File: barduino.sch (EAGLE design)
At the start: 17 parts, among them Q2 16MHz, X1 MINI-USB-UX60A-MB-5ST

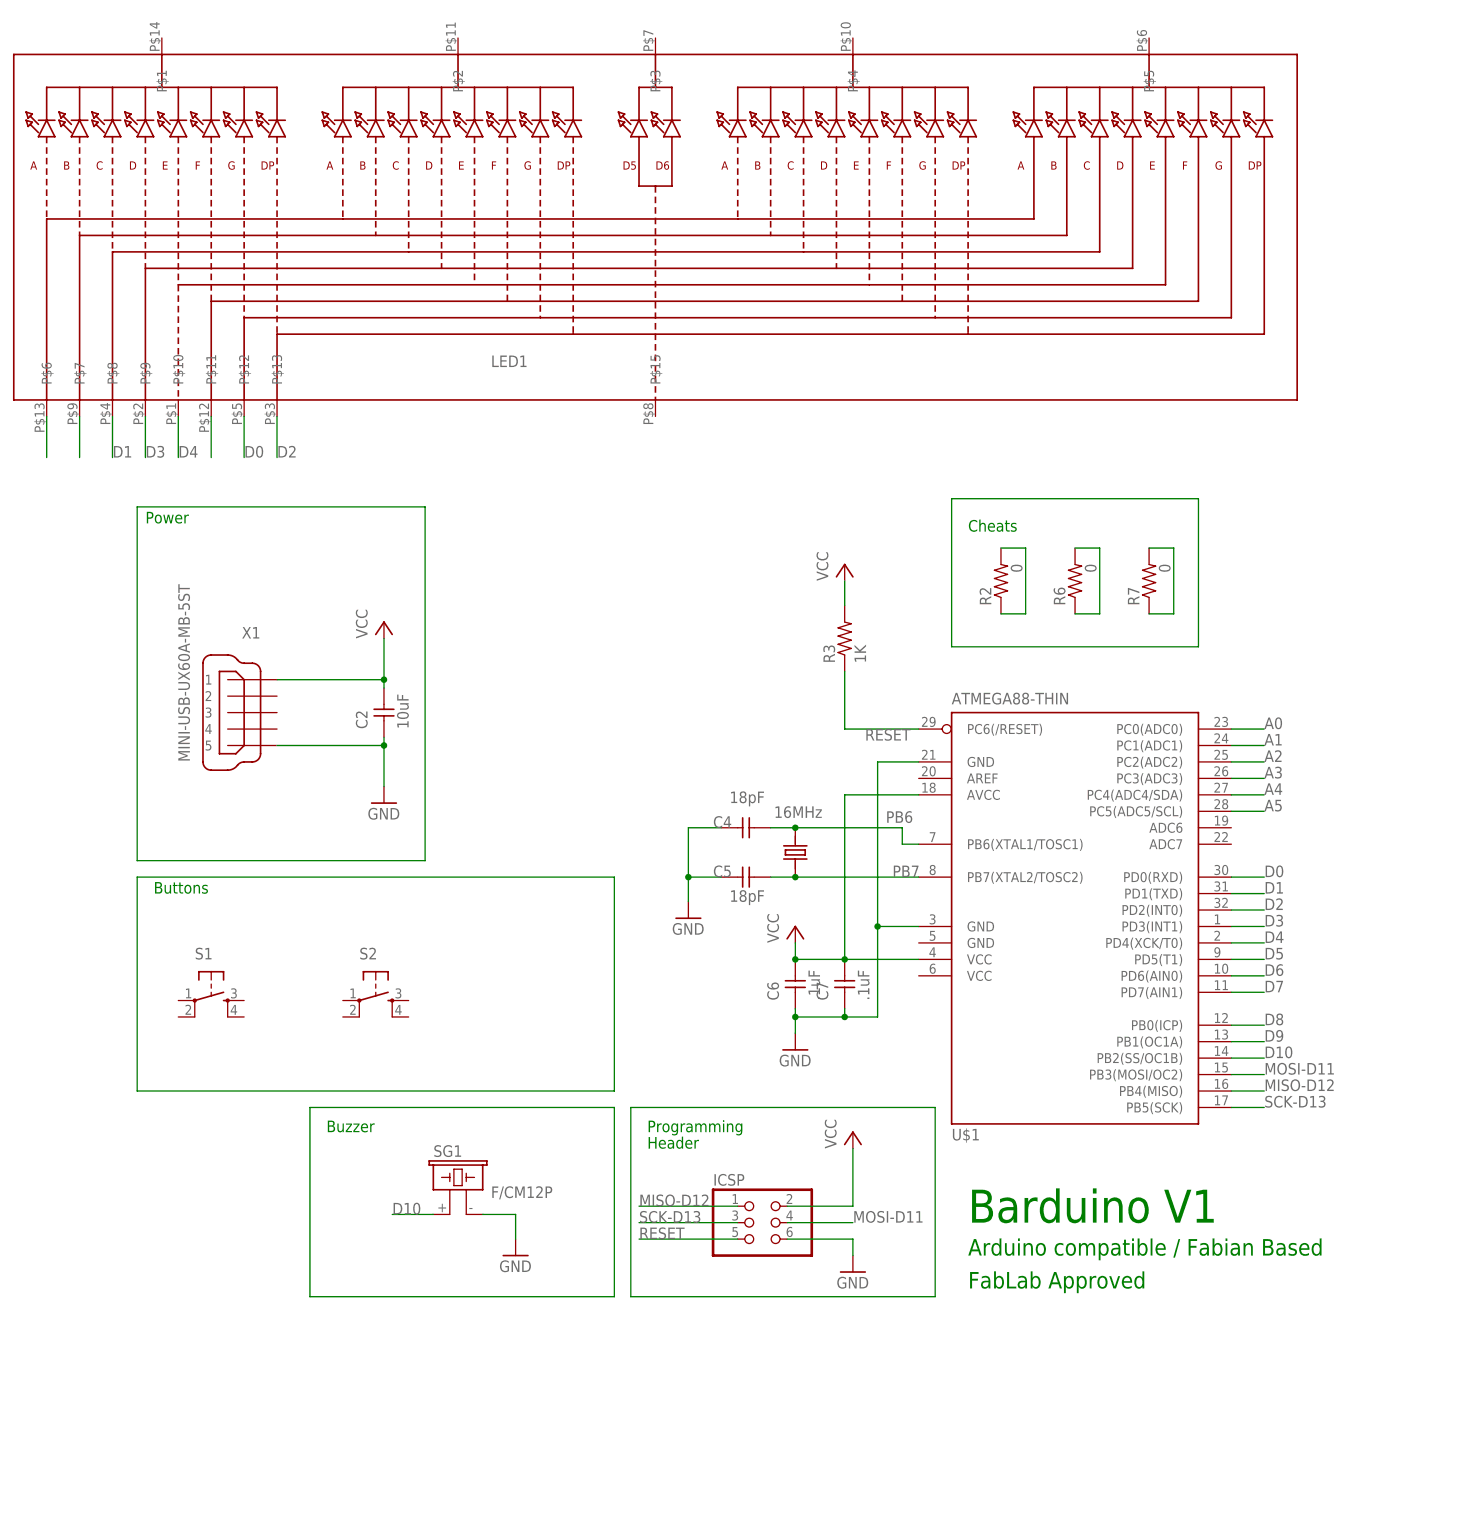
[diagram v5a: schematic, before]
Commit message: replace clock part with 2 custom headers
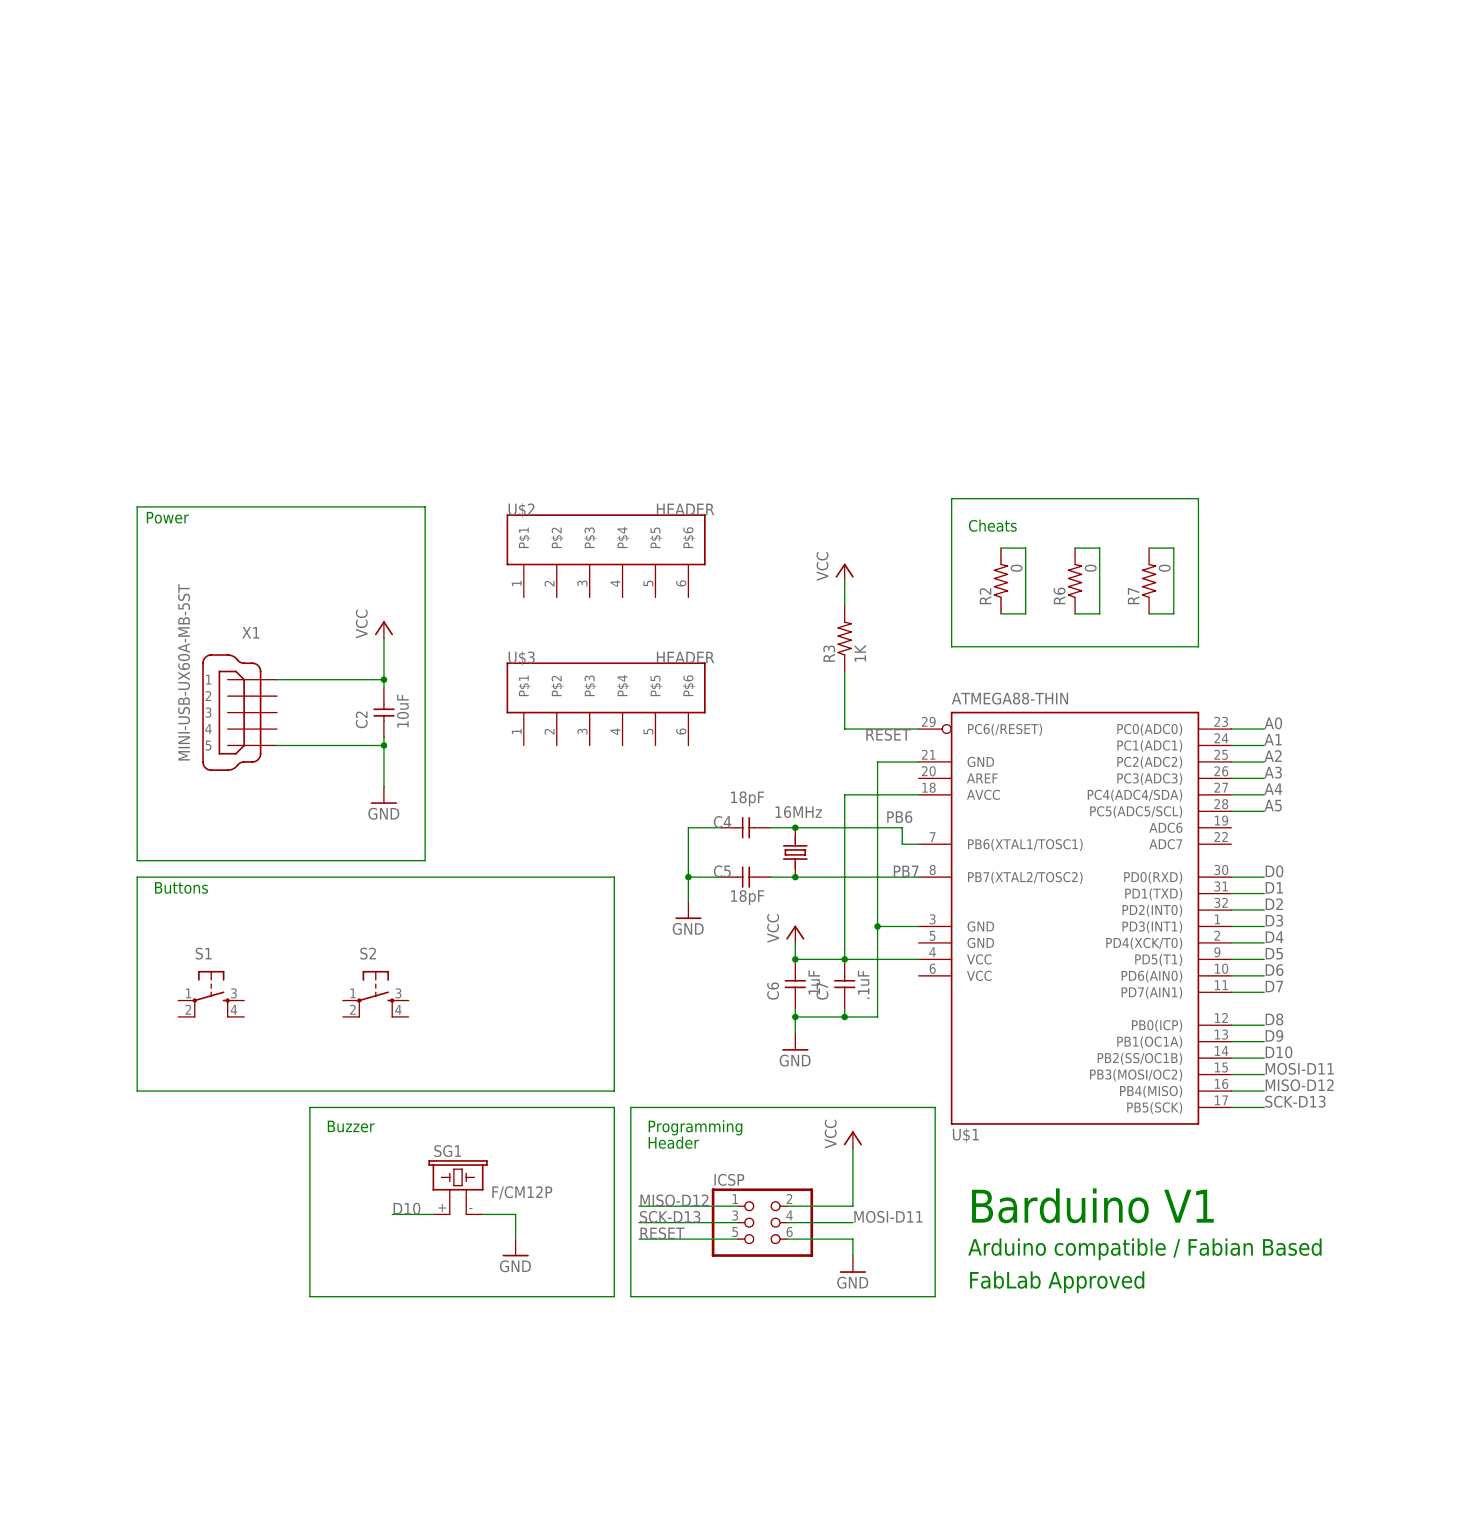
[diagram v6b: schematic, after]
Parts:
- removed LED1: (no value), microbuilder:DISP_SEGMENT_4DIGIT_BL-Q56C43
- added U$2, U$3: HEADER, 4-Digit-Clock:HEADER
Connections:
- removed net N$22: LED1.P$6
- removed net N$23: LED1.P$7
- removed net N$27: LED1.P$11
- net D0: no longer LED1.P$12
- net D1: no longer LED1.P$8
- net D2: no longer LED1.P$13
- net D3: no longer LED1.P$9
- net D4: no longer LED1.P$10
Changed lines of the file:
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@@
 <setting verticaltext="up"/>
 </settings>
-<grid distance="0.05" unitdist="inch" unit="inch" style="lines" multiple="1" display="no" altdistance="0.01" altunitdist="inch" altunit="inch"/>
+<grid distance="0.1" unitdist="inch" unit="inch" style="lines" multiple="1" display="no" altdistance="0.01" altunitdist="inch" altunit="inch"/>
 <layers>
 <layer number="1" name="Top" color="4" fill="1" visible="no" active="no"/>
@@
 <part name="R7" library="ng" deviceset="RESISTOR" device="1206" value="0"/>
 <part name="R2" library="ng" deviceset="RESISTOR" device="1206" value="0"/>
-<part name="LED1" library="microbuilder" deviceset="DISP_SEGMENT_4DIGIT_BL-Q56C43" device=""/>
 <part name="GND2" library="supply1" library_urn="urn:adsk.eagle:library:371" deviceset="GND" device=""/>
 <part name="SG1" library="buzzer" library_urn="urn:adsk.eagle:library:113" deviceset="F/CM12P" device=""/>
@@
 <part name="P+4" library="supply1" library_urn="urn:adsk.eagle:library:371" deviceset="VCC" device=""/>
 <part name="GND5" library="supply1" library_urn="urn:adsk.eagle:library:371" deviceset="GND" device=""/>
+<part name="U$2" library="4-Digit-Clock" deviceset="HEADER" device=""/>
+<part name="U$3" library="4-Digit-Clock" deviceset="HEADER" device=""/>
 </parts>
 <sheets>
@@
 <attribute name="VALUE" x="84.582" y="120.65" size="1.778" layer="96" rot="R90"/>
 </instance>
-<instance part="LED1" gate="G$1" x="27.94" y="170.18"/>
 <instance part="GND2" gate="1" x="6.35" y="15.24"/>
 <instance part="SG1" gate="G$1" x="-3.81" y="24.13"/>
@@
 <instance part="P+4" gate="VCC" x="58.42" y="34.29"/>
 <instance part="GND5" gate="1" x="58.42" y="12.7"/>
+<instance part="U$2" gate="G$1" x="20.32" y="127"/>
+<instance part="U$3" gate="G$1" x="20.32" y="104.14"/>
 </instances>
 <busses>
@@
 <pinref part="U$1" gate="G$1" pin="PD0(RXD)"/>
 </segment>
-<segment>
-<pinref part="LED1" gate="G$1" pin="P$12"/>
-<wire x1="-35.56" y1="144.78" x2="-35.56" y2="138.43" width="0.1524" layer="91"/>
-<label x="-35.56" y="138.43" size="1.778" layer="95"/>
-</segment>
 </net>
 <net name="D1" class="0">
@@
 <pinref part="U$1" gate="G$1" pin="PD1(TXD)"/>
 </segment>
-<segment>
-<pinref part="LED1" gate="G$1" pin="P$8"/>
-<wire x1="-55.88" y1="144.78" x2="-55.88" y2="138.43" width="0.1524" layer="91"/>
-<label x="-55.88" y="138.43" size="1.778" layer="95"/>
-</segment>
 </net>
 <net name="D2" class="0">
@@
 <pinref part="U$1" gate="G$1" pin="PD2(INT0)"/>
 </segment>
-<segment>
-<pinref part="LED1" gate="G$1" pin="P$13"/>
-<wire x1="-30.48" y1="144.78" x2="-30.48" y2="138.43" width="0.1524" layer="91"/>
-<label x="-30.48" y="138.43" size="1.778" layer="95"/>
-</segment>
 </net>
 <net name="D3" class="0">
@@
 <pinref part="U$1" gate="G$1" pin="PD3(INT1)"/>
 </segment>
-<segment>
-<pinref part="LED1" gate="G$1" pin="P$9"/>
-<wire x1="-50.8" y1="144.78" x2="-50.8" y2="138.43" width="0.1524" layer="91"/>
-<label x="-50.8" y="138.43" size="1.778" layer="95"/>
-</segment>
 </net>
 <net name="D4" class="0">
@@
 <label x="121.92" y="63.5" size="1.778" layer="95"/>
 <pinref part="U$1" gate="G$1" pin="PD4(XCK/T0)"/>
-</segment>
-<segment>
-<pinref part="LED1" gate="G$1" pin="P$10"/>
-<wire x1="-45.72" y1="144.78" x2="-45.72" y2="138.43" width="0.1524" layer="91"/>
-<label x="-45.72" y="138.43" size="1.778" layer="95"/>
 </segment>
 </net>
@@
 </segment>
 </net>
-<net name="N$22" class="0">
-<segment>
-<pinref part="LED1" gate="G$1" pin="P$6"/>
-<wire x1="-66.04" y1="144.78" x2="-66.04" y2="138.43" width="0.1524" layer="91"/>
-</segment>
-</net>
-<net name="N$23" class="0">
-<segment>
-<pinref part="LED1" gate="G$1" pin="P$7"/>
-<wire x1="-60.96" y1="144.78" x2="-60.96" y2="138.43" width="0.1524" layer="91"/>
-</segment>
-</net>
-<net name="N$27" class="0">
-<segment>
-<pinref part="LED1" gate="G$1" pin="P$11"/>
-<wire x1="-40.64" y1="144.78" x2="-40.64" y2="138.43" width="0.1524" layer="91"/>
-</segment>
-</net>

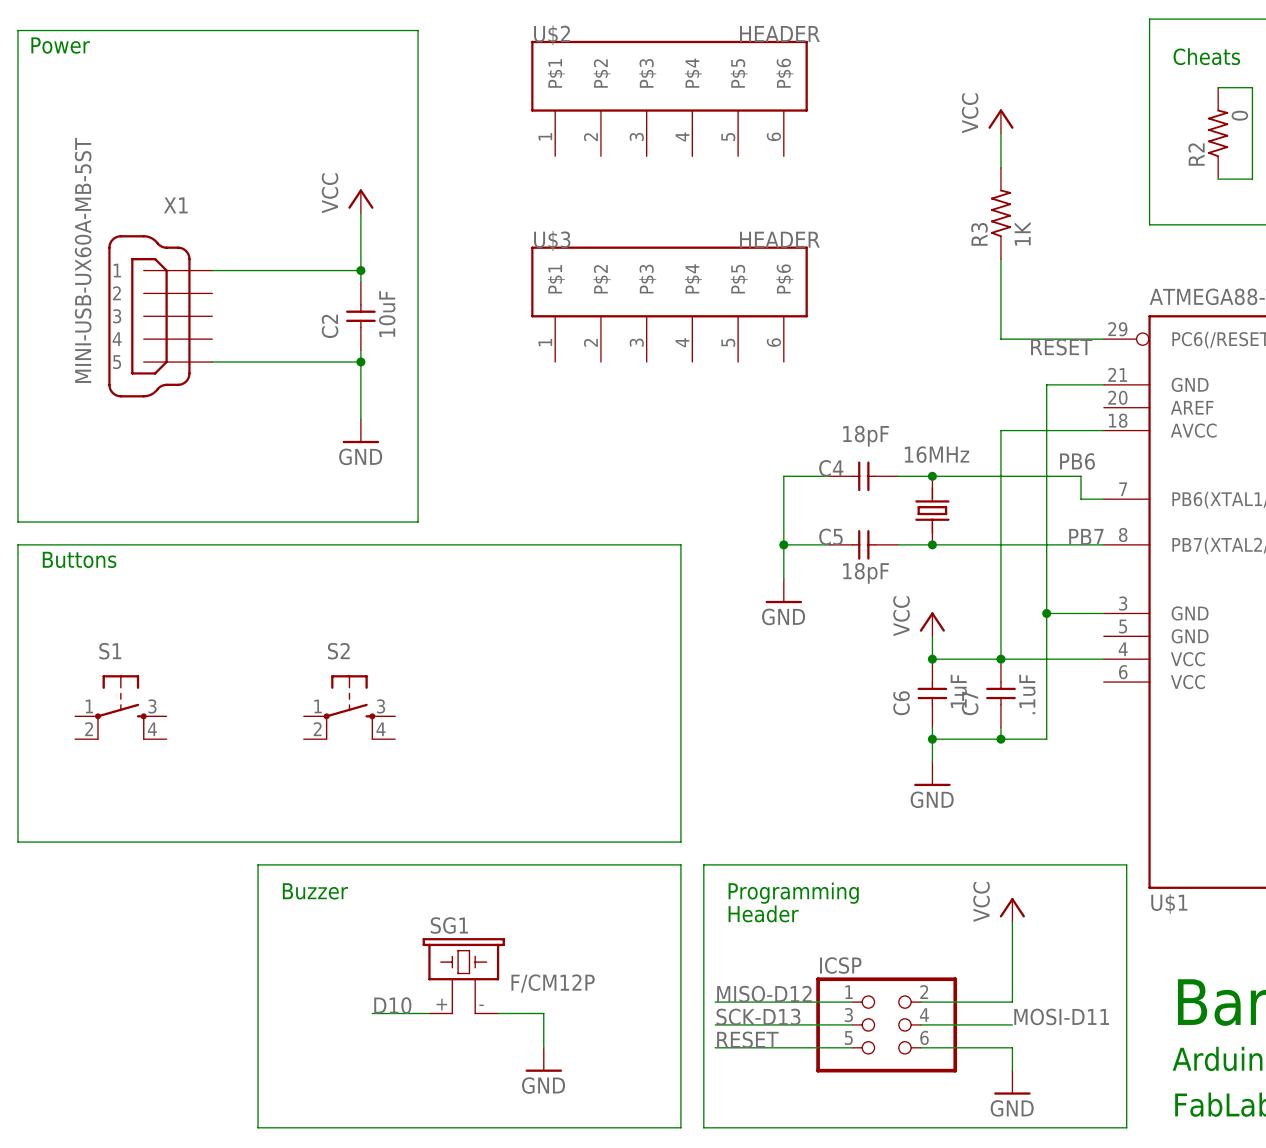
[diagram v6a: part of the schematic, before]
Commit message: display and buttons connected
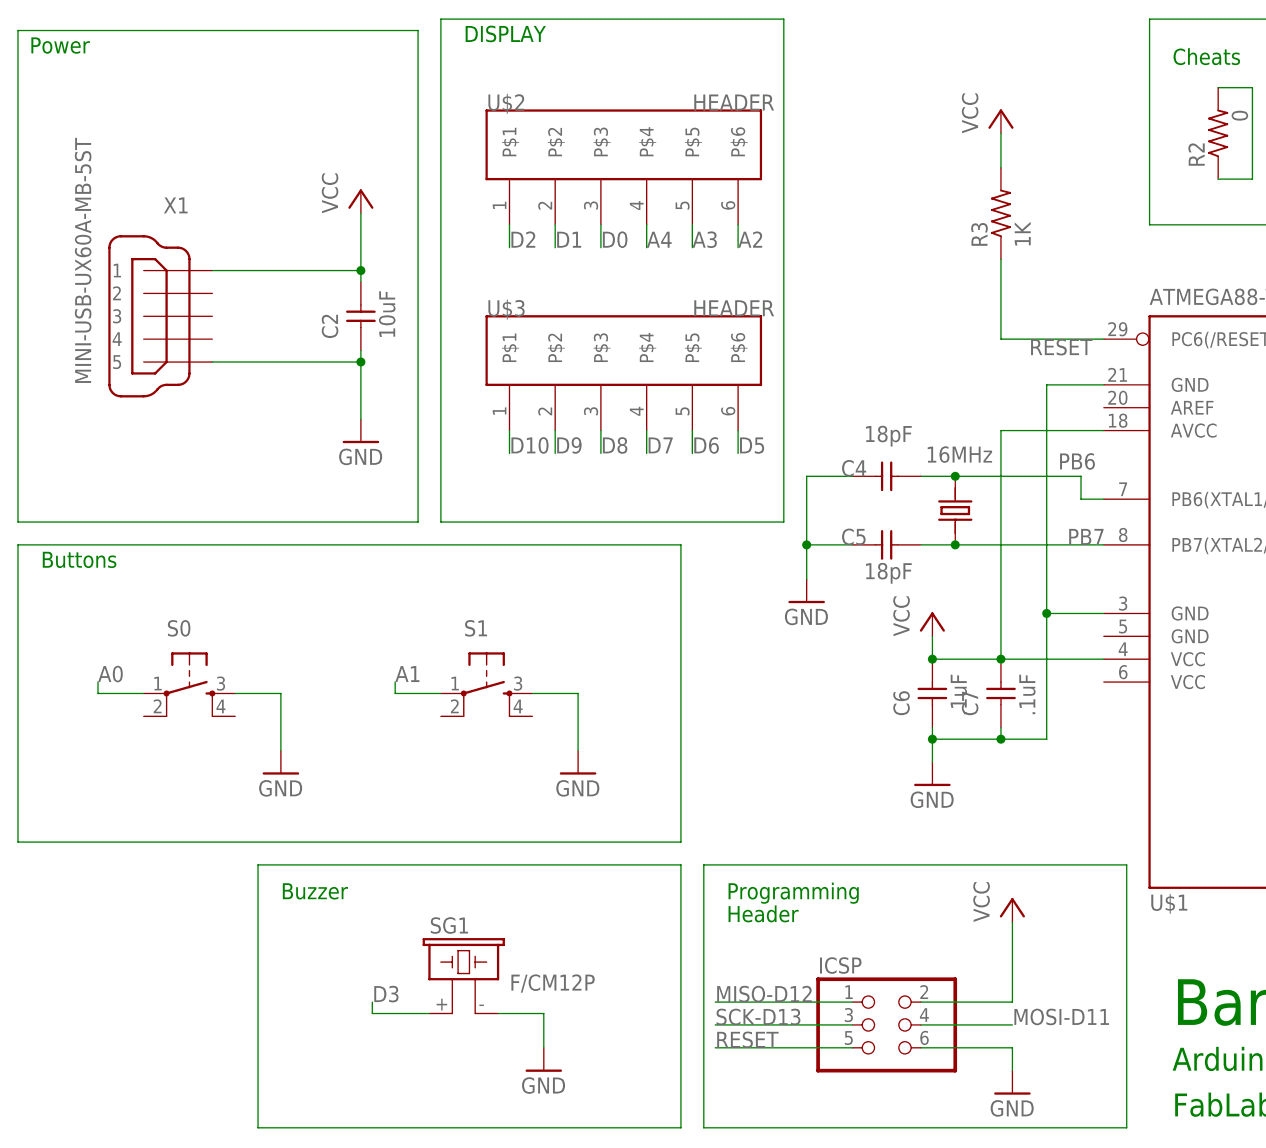
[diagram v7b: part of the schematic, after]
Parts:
- removed S2: (no value), ng:6MM_SWITCH6MM_SWITCH
- added S0: (no value), ng:6MM_SWITCH6MM_SWITCH
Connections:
- net A0: now also S0.P
- net A1: now also S1.P
- net A2: now also U$2.P$6
- net A3: now also U$2.P$5
- net A4: now also U$2.P$4
- net D0: now also U$2.P$3
- net D1: now also U$2.P$2
- net D10: now also U$3.P$1; no longer SG1.1
- net D2: now also U$2.P$1
- net D3: now also SG1.1
- net D5: now also U$3.P$6
- net D6: now also U$3.P$5
- net D7: now also U$3.P$4
- net D8: now also U$3.P$3
- net D9: now also U$3.P$2
- net GND: now also S0.S, S1.S
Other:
- note added: "DISPLAY"
- moved on the sheet: C4, C5, S1, U$2, U$3

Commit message: lots of routing
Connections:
- removed net N$3: R6.1, R6.2
- net SCK-D13: no longer R2.1, R2.2
- net VCC: no longer R7.1, R7.2
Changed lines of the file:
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@@
-</segment>
-<segment>
-<pinref part="R7" gate="G$1" pin="1"/>
-<wire x1="104.14" y1="114.3" x2="107.95" y2="114.3" width="0.1524" layer="91"/>
-<wire x1="107.95" y1="114.3" x2="107.95" y2="124.46" width="0.1524" layer="91"/>
-<pinref part="R7" gate="G$1" pin="2"/>
-<wire x1="107.95" y1="124.46" x2="104.14" y2="124.46" width="0.1524" layer="91"/>
 </segment>
 <segment>
@@
 <pinref part="ICSP" gate="A" pin="3"/>
 </segment>
-<segment>
-<pinref part="R2" gate="G$1" pin="1"/>
-<wire x1="81.28" y1="114.3" x2="85.09" y2="114.3" width="0.1524" layer="91"/>
-<wire x1="85.09" y1="114.3" x2="85.09" y2="124.46" width="0.1524" layer="91"/>
-<pinref part="R2" gate="G$1" pin="2"/>
-<wire x1="85.09" y1="124.46" x2="81.28" y2="124.46" width="0.1524" layer="91"/>
-</segment>
 </net>
 <net name="N$8" class="0">
@@
 </segment>
 </net>
-<net name="N$3" class="0">
-<segment>
-<pinref part="R6" gate="G$1" pin="1"/>
-<pinref part="R6" gate="G$1" pin="2"/>
-<wire x1="92.71" y1="124.46" x2="96.52" y2="124.46" width="0.1524" layer="91"/>
-<wire x1="96.52" y1="124.46" x2="96.52" y2="114.3" width="0.1524" layer="91"/>
-<wire x1="96.52" y1="114.3" x2="92.71" y2="114.3" width="0.1524" layer="91"/>
-</segment>
-</net>
